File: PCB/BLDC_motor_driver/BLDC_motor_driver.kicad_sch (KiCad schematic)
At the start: 4 parts, among them U2 AS5048A, U5 SN65HVD230, U6 STM32F405RGTx, U7 STM32F303K8Tx

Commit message: pcb progress
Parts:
- removed U2: AS5048A, Package_SO:TSSOP-14_4.4x5mm_P0.65mm, symbol Sensor_Magnetic:AS5048A
- removed U7: STM32F303K8Tx, Package_QFP:LQFP-32_7x7mm_P0.8mm, symbol MCU_ST_STM32F3:STM32F303K8Tx
- added U10: AS5048A, Package_SO:TSSOP-14_4.4x5mm_P0.65mm, symbol Sensor_Magnetic:AS5048A
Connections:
- net STM2_CAN_TX: now reaches U5.1 (D)
- net STM2_CAN_TX: now also U6.45 (PA12)
- net STM2_CAN_RX: now reaches U5.4 (R)
- net STM2_CAN_RX: now also U6.44 (PA11)
- net STM2_SPI1_SCK: now reaches U6.21 (PA5)
- net STM2_SPI1_SCK: now also U10.2 (CLK)
- net STM2_SPI1_MISO: now reaches U6.22 (PA6)
- net STM2_SPI1_MISO: now also U10.3 (MISO)
- net STM2_SPI1_MOSI: now reaches U6.23 (PA7)
- net STM2_SPI1_MOSI: now also U10.4 (MOSI)
- net STM2_SPI1_CS: now reaches U6.24 (PC4)
- net STM2_SPI1_CS: now also U10.1 (~{CSn})
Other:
- sheet BLDC driver renamed BLDC driver phase A
- added sheet STM32F303KBT6 (STM32F303KBT6.kicad_sch)
- sheet BLDC driver phase A: file untitled.kicad_sch -> BLDC_driver_phaseA.kicad_sch
- sheet BLDC driver phase A ports: added PHASE A, PWM_IN_A, PWR_12V, PWR_3.3V, SD_A, VISENSE_A; removed none
- moved on the sheet: U5, U6

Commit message: updated schematic
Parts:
- added C10, C11, C12, C3, C9: C, symbol Device:C
- added C4, C5, C6, C7, C8: C_Small, symbol Device:C_Small
- added Y1: 8MHz, Crystal:Crystal_SMD_EuroQuartz_MJ-4Pin_5.0x3.2mm, symbol Device:Crystal_GND24
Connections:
- net +3V3: now reaches U10.12 (VDD3V)
- net +3V3: now also C3.1
- net GND: now reaches U10.13 (GND)
- net GND: now also U6.12 (VSSA), U6.18 (VSS), U6.63 (VSS), C10.2, C11.2, C12.2, C3.2, C9.2, Y1.2, Y1.4
- net at U6.31 (VCAP_1): now also C12.1
- net at U6.47 (VCAP_2): now also C11.1
- net at U6.5 (PH0): now also C10.1, Y1.1
- net at U6.6 (PH1): now also C9.1, Y1.3
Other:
- sheet BLDC driver phase A: file BLDC_driver_phaseA.kicad_sch -> untitled.kicad_sch

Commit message: updated schematic
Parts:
- removed C4, C5, C6, C7, C8: C_Small, symbol Device:C_Small
- added C13: C, symbol Device:C
- added C14, C15, C16, C17: 100n, symbol Device:C
- added C18: 10n, symbol Device:C
- added C19, C21: 1u, symbol Device:C
- added C20: 10u, symbol Device:C
- added C5: 100n, Capacitor_SMD:C_0504_1310Metric, symbol Device:C
- added FB1: 120R, symbol Device:FerriteBead
- added J2: Screw_Terminal_01x02, TerminalBlock:TerminalBlock_Xinya_XY308-2.54-2P_1x02_P2.54mm_Horizontal, symbol Connector:Screw_Terminal_01x02
- added J3: Conn_01x04_Socket, Connector_PinHeader_2.54mm:PinHeader_1x04_P2.54mm_Vertical, symbol Connector:Conn_01x04_Socket
- added R5: R, symbol Device:R
- added R6: 120R, Resistor_SMD:R_0402_1005Metric, symbol Device:R
- C10, C9: value C -> 15p; footprint (none) -> Capacitor_SMD:C_0603_1608Metric
- C3: value C -> 10u; footprint (none) -> Capacitor_SMD:C_0504_1310Metric
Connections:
- net +3V3 is gone; now on net +3.3V: C3.1, U10.12 (VDD3V)
- net GND: now also C10.1, U10.10 (TEST), U10.5 (TEST), U10.6 (TEST), U10.7 (TEST), U10.8 (TEST), U10.9 (TEST), U5.2 (GND), C13.2, C14.2, C15.2, C16.2, C17.2, C18.2, C19.2, C20.2, C21.2, C5.2; no longer C10.2
- net at U6.5 (PH0), Y1.1: now also C10.2; no longer C10.1
- net +3.3V: now reaches U5.3 (VCC)
- net +3.3V: now also U10.11 (VDD5V), U5.5 (Vref), U6.1 (VBAT), U6.19 (VDD), U6.32 (VDD), U6.48 (VDD), U6.64 (VDD), C14.1, C15.1, C16.1, C17.1, C20.1, C5.1, R5.1
- net at U5.6 (CANL): now also J2.2 (Pin_2), R6.2
- net at U5.7 (CANH): now also J2.1 (Pin_1), R6.1
- net +3.3VA: now reaches U6.13 (VDDA)
- net +3.3VA: now also C18.1, C19.1, C21.1, FB1.1, FB1.2
- net at U6.7 (NRST): now also C13.1, R5.2
- no-connect marks 0 -> 1
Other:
- moved on the sheet: C10, C11, C12, C3, C9, U10, U5, U6, Y1

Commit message: more pcb progress
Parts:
- removed C11, C12: C, symbol Device:C
- removed J3: Conn_01x04_Socket, Connector_PinHeader_2.54mm:PinHeader_1x04_P2.54mm_Vertical, symbol Connector:Conn_01x04_Socket
- added C22, C23: 100n, symbol Device:C
- added C6, C7: 22u, Capacitor_SMD:C_0504_1310Metric, symbol Device:C
- added D2: LED, LED_SMD:LED_0402_1005Metric, symbol Device:LED
- added H1, H2, H3, H4: MountingHole, MountingHole:MountingHole_2.2mm_M2, symbol Mechanical:MountingHole
- added J1: Current Sensing, TerminalBlock:TerminalBlock_Xinya_XY308-2.54-3P_1x03_P2.54mm_Horizontal, symbol Connector:Screw_Terminal_01x03
- added J3: PWR, TerminalBlock:TerminalBlock_Xinya_XY308-2.54-2P_1x02_P2.54mm_Horizontal, symbol Connector:Screw_Terminal_01x02
- added J4: Conn_01x04_Socket, Connector_PinSocket_2.54mm:PinSocket_1x04_P2.54mm_Horizontal, symbol Connector:Conn_01x04_Socket
- added R7: 1k5, Resistor_SMD:R_0402_1005Metric, symbol Device:R
- added U11: AMS1117-3.3, Package_TO_SOT_SMD:SOT-223-3_TabPin2, symbol Regulator_Linear:AMS1117-3.3
- C20: value 10u -> 4.7u
- J2: value Screw_Terminal_01x02 -> CAN H/L
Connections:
- net +3.3V: now also C7.1, D2.2 (A), U11.2 (VO)
- net +3.3VA: now also J4.4 (Pin_4)
- net GND: now also C22.2, C23.2, C6.2, C7.2, J3.2 (Pin_2), J4.2 (Pin_2), R7.2, U11.1 (GND)
- net at U6.47 (VCAP_2): now also C23.1
- net at U6.31 (VCAP_1): now also C22.1
- net SWDIO: now reaches U6.46 (PA13)
- net SWDIO: now also J4.1 (Pin_1)
- net SWCLK: now reaches U6.49 (PA14)
- net SWCLK: now also J4.3 (Pin_3)
- net BOOT0: now reaches U6.60 (BOOT0)
- net STM2_CAN_RX renamed CAN_RX
- net STM2_CAN_TX renamed CAN_TX
- net STM2_SPI1_CS renamed SPI1_CS
- net STM2_SPI1_MISO renamed SPI1_MISO
- net STM2_SPI1_MOSI renamed SPI1_MOSI
- net STM2_SPI1_SCK renamed SPI1_SCK
- new net: D2.1 (K), R7.1
- new net +5V: C6.1, J3.1 (Pin_1), U11.3 (VI)
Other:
- removed sheet STM32F303KBT6
- moved on the sheet: J2, R6, U5

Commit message: more progress
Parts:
- added C11, C12: 15p, Capacitor_SMD:C_0603_1608Metric, symbol Device:C
- added C24, C28: 100n, symbol Device:C
- added C27: 100n, Capacitor_SMD:C_0504_1310Metric, symbol Device:C
- added C8: 1u, Capacitor_SMD:C_0504_1310Metric, symbol Device:C
- added R8: 4k7, symbol Device:R
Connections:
- net +3.3V: now also C21.1, FB1.2, J4.1 (Pin_1), C24.1, C27.1, C28.1, C8.1; no longer U5.5 (Vref)
- net +3.3VA: no longer C21.1, FB1.2, J4.4 (Pin_4)
- net GND: now also J4.4 (Pin_4), C11.2, C12.2, C24.2, C27.2, C28.2, C8.2, R8.2; no longer J4.2 (Pin_2)
- net SWDIO: now also J4.2 (Pin_2); no longer J4.1 (Pin_1)
- net at J2.2 (Pin_2), R6.2, U5.6 (CANL): now also C12.1
- net at J2.1 (Pin_1), R6.1, U5.7 (CANH): now also C11.1
- net at U5.8 (Rs): now also R8.1
- net BOOT1: now reaches U6.28 (PB2)
- no-connect marks 1 -> 2
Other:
- moved on the sheet: C14, C15, C16, C17, C20, C3, C5, C6, J1, J2, R6, U10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

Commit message: further PCB progress
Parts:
- removed C11, C12: 15p, Capacitor_SMD:C_0603_1608Metric, symbol Device:C
- removed C6, C7: 22u, Capacitor_SMD:C_0504_1310Metric, symbol Device:C
- added C29, C4: 100n, Capacitor_SMD:C_0504_1310Metric, symbol Device:C
- added C6, C7: 22u, symbol Device:C_Polarized
- added L2: L_Ferrite_Coupled_1324, Inductor_SMD:L_CommonModeChoke_Coilcraft_1812CAN, symbol Device:L_Ferrite_Coupled_1324
- C13, C14, C15, C16, C17, C18, C19, C20, C21, C22, C23, C28: footprint (none) -> Capacitor_SMD:C_0201_0603Metric
- FB1: footprint (none) -> Inductor_SMD:L_Walsin_WLFM201209x
- J2: value CAN H/L -> PWR
- J3: value PWR -> CAN H/L
- R5: footprint (none) -> Resistor_SMD:R_0402_1005Metric
- R7: value 1k5 -> 100R
- R8: value 4k7 -> 0R
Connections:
- net +3.3V: now also C29.1, C6.1
- net +5V: now also J2.2 (Pin_2), C4.1, C7.1; no longer J3.1 (Pin_1)
- net GND: now also J2.1 (Pin_1), C29.2, C4.2, C6.2, C7.2; no longer J3.2 (Pin_2)
- new net: J3.1 (Pin_1), L2.3, R6.1
- new net: J3.2 (Pin_2), L2.4, R6.2
- new net: L2.2, U5.6 (CANL)
- new net: L2.1, U5.7 (CANH)
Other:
- sheet BLDC driver phase A ports: added none; removed PHASE A
- moved on the sheet: C14, C15, C16, C17, C20, C24, C28, D2, H1, H2, H3, H4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

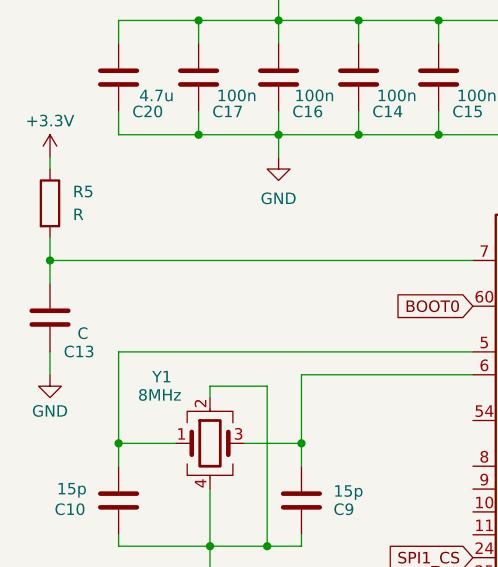
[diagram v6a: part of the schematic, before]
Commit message: PCB schematic progress - footprints and values
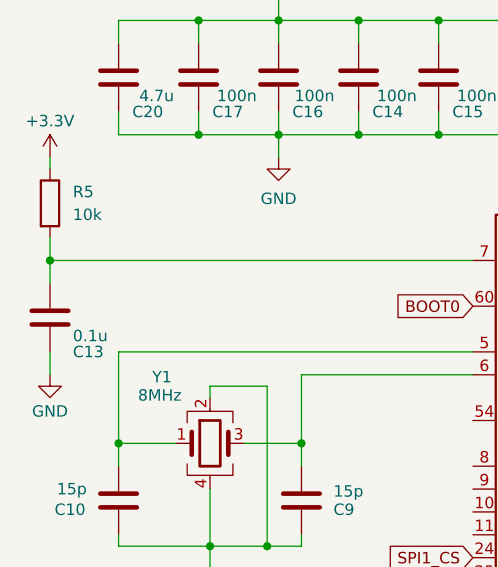
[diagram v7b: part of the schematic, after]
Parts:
- C13: value C -> 0.1u
- R5: value R -> 10k
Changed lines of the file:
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@@
 			)
 		)
-		(property "Value" "R"
+		(property "Value" "10k"
 			(at 22.86 58.4199 0)
 			(effects
@@
 		(dnp no)
 		(property "Reference" "C13"
-			(at 21.844 73.66 0)
+			(at 22.86 73.66 0)
 			(effects
 				(font
@@
 			)
 		)
-		(property "Value" "C"
-			(at 23.368 71.628 0)
+		(property "Value" "0.1u"
+			(at 22.86 71.882 0)
 			(effects
 				(font

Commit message: PCB v2 progress...
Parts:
- added C12: 22u, Capacitor_Tantalum_SMD:CP_EIA-2012-12_Kemet-R, symbol Device:C_Polarized
- added H5: 12V, MountingHole:MountingHole_2.2mm_M2_Pad_TopBottom, symbol Mechanical:MountingHole_Pad
- added H6: GND, MountingHole:MountingHole_2.2mm_M2_Pad_TopBottom, symbol Mechanical:MountingHole_Pad
- C10, C9: footprint Capacitor_SMD:C_0603_1608Metric -> Capacitor_SMD:C_0402_1005Metric
- C13, C14, C15, C16, C17, C18, C19, C20, C21, C22, C23, C28: footprint Capacitor_SMD:C_0201_0603Metric -> Capacitor_SMD:C_0402_1005Metric
- C24: footprint (none) -> Capacitor_SMD:C_0402_1005Metric
- C27, C29, C3, C4, C5, C8: footprint Capacitor_SMD:C_0504_1310Metric -> Capacitor_SMD:C_0402_1005Metric
- R8: footprint (none) -> Resistor_SMD:R_0402_1005Metric
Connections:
- net GND: now also C12.2, H6.1
- new net +12V: C12.1, H5.1
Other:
- sheet BLDC driver phase A ports: added GND; removed none
- moved on the sheet: C22
